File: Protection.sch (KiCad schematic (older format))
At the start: 11 parts, among them Q1 MMBT3906, U1 TLVH431

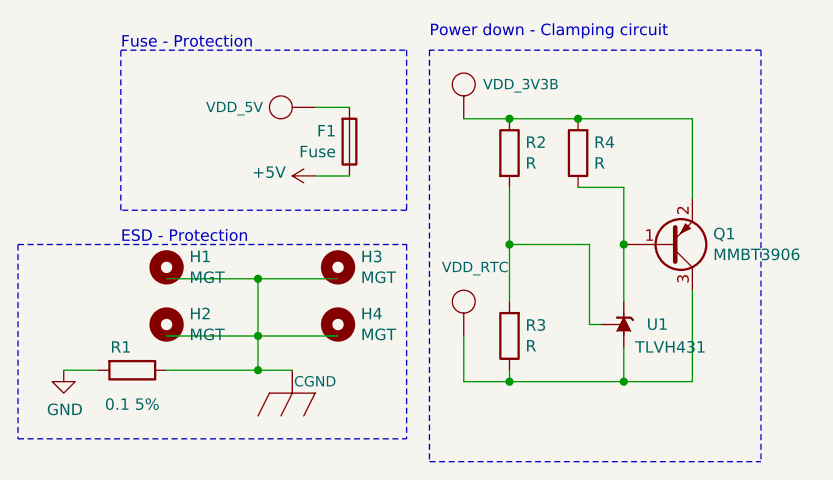
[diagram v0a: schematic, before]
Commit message: Bill of Materials + Some 3D Models
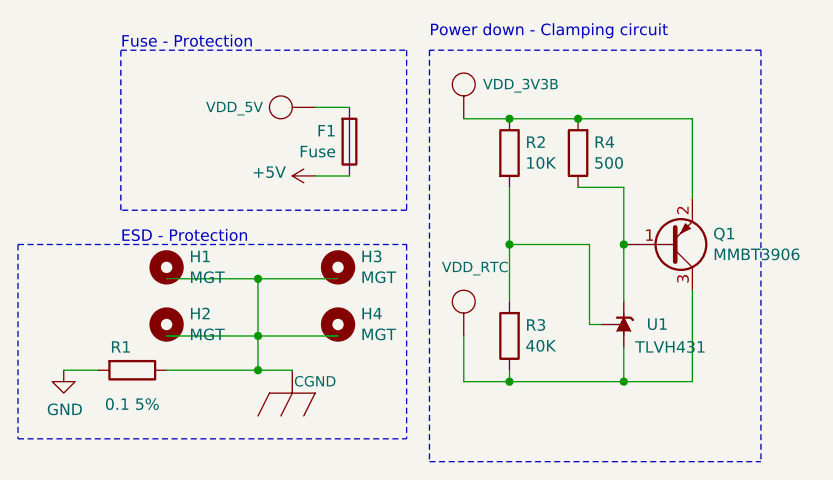
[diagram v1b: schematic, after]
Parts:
- R2: value R -> 10K
- R3: value R -> 40K
- R4: value R -> 500
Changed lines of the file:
@@
 AR Path="/5F9E362C/5FA066F5" Ref="R4"  Part="1"
 F 0 "R4" H 6180 3204 50  0000 R CNN
-F 1 "R" H 6180 3295 50  0000 R CNN
+F 1 "500" H 6180 3295 50  0000 R CNN
 F 2 "Resistor_SMD:R_0603_1608Metric" V 6180 3250 50  0001 C CNN
 F 3 "~" H 6250 3250 50  0001 C CNN
@@
 AR Path="/5F9E362C/5FA06765" Ref="R2"  Part="1"
 F 0 "R2" H 6020 3296 50  0000 L CNN
-F 1 "R" H 6020 3205 50  0000 L CNN
+F 1 "10K" H 6020 3205 50  0000 L CNN
 F 2 "Resistor_SMD:R_0603_1608Metric" V 5880 3250 50  0001 C CNN
 F 3 "~" H 5950 3250 50  0001 C CNN
@@
 AR Path="/5F9E362C/5FA0676B" Ref="R3"  Part="1"
 F 0 "R3" H 5880 4004 50  0000 R CNN
-F 1 "R" H 5880 4095 50  0000 R CNN
+F 1 "40K" H 5880 4095 50  0000 R CNN
 F 2 "Resistor_SMD:R_0603_1608Metric" V 5880 4050 50  0001 C CNN
 F 3 "~" H 5950 4050 50  0001 C CNN

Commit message: DRC Fixes and more
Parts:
- F1: footprint Fuse:Fuse_Littelfuse-NANO2-451_453 -> footprints:FUSC6125X279N
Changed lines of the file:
@@
 F 0 "F1" H 5191 3154 50  0000 R CNN
 F 1 "Fuse" H 5191 3245 50  0000 R CNN
-F 2 "Fuse:Fuse_Littelfuse-NANO2-451_453" V 5180 3200 50  0001 C CNN
+F 2 "footprints:FUSC6125X279N" V 5180 3200 50  0001 C CNN
 F 3 "~" H 5250 3200 50  0001 C CNN
 	1    5250 3200
